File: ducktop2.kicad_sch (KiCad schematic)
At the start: 0 parts

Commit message: Checkpoint ducktop2 generated schematic baseline
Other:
- added sheet Ham Radio (09_ham_radio.kicad_sch)
- added sheet Intehill Monitor Interface (11_intehill_monitor_interface.kicad_sch)
- added sheet Internal Display (10_internal_display.kicad_sch)
- added sheet Internal Services (08_internal_services.kicad_sch)
- added sheet Keyboard Daughterboard (12_keyboard_daughterboard.kicad_sch)
- added sheet Maker MCU (14_maker_mcu.kicad_sch)
- added sheet Mu Carrier (03_mu_carrier.kicad_sch)
- added sheet Power Inputs (05_power_inputs.kicad_sch)
- added sheet Radio Audio Codec (13_radio_audio_codec.kicad_sch)
- added sheet Radio/OLED/GNSS (07_radio_oled_gps.kicad_sch)
- added sheet TCP0 External HDMI (06_tcp0_external_hdmi.kicad_sch)
- added sheet USB-C Hub I/O (04_usb_c_io.kicad_sch)
- sheet EC & MCU ports: added AUX_DC_ADC, FAN_PWM, FAN_TACH, GNSS_EXTINT, GNSS_PPS, GNSS_RESET_N, GNSS_UART_RX, GNSS_UART_TX, KB_COL0, KB_COL1, KB_COL10, KB_COL11, KB_COL12, KB_COL13, KB_COL14, KB_COL15, KB_COL2, KB_COL3, KB_COL4, KB_COL5, KB_COL6, KB_COL7, KB_COL8, KB_COL9, KB_ROW0, KB_ROW1, KB_ROW2, KB_ROW3, KB_ROW4, KB_ROW5, KB_ROW6, KB_ROW7, LCD_BL_EN, LCD_BL_PWM, LID_CLOSED_N, MU_PWRBTN_N, MU_RSTBTN_N, OLED_RESET_N, PANEL_PWR_EN, PANEL_RESET_N, RADIO_AUDIO_SEL, RADIO_GPIO0, RADIO_UHF_PD_N, RADIO_UHF_PTT_N, RADIO_UHF_RF_SEL, RADIO_UHF_SQL, RADIO_UHF_UART_RX, RADIO_UHF_UART_TX, RADIO_VHF_PD_N, RADIO_VHF_PTT_N, RADIO_VHF_RF_SEL, RADIO_VHF_SQL, RADIO_VHF_UART_RX, RADIO_VHF_UART_TX, THERM_MU_ADC, THERM_SKIN_ADC, TOUCH_INT_N, TOUCH_RESET_N, TPAD_INT_N, TPAD_RESET_N, WIFI_W_DISABLE1_N, WIFI_W_DISABLE2_N; removed none
- sheet Power & Battery ports: added AUX_DC_ADC, MCU_3V3; removed none

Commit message: Publish the current Ducktop2 design
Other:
- sheet USB-C Hub I/O renamed Native USB-C I/O
- removed sheet Intehill Monitor Interface
- removed sheet Internal Display
- removed sheet Keyboard Daughterboard
- added sheet Gigabit Ethernet (16_gigabit_ethernet.kicad_sch)
- added sheet Keyboard Mainboard FFC (12_keyboard_interface.kicad_sch)
- added sheet System Audio (15_system_audio.kicad_sch)
- sheet EC & MCU ports: added AON_FAULT_N, AUDIO_AMP_EC_EN, AUDIO_MIC_EN, AUX_FAULT_N, AUX_PGOOD, CASE_PWRBTN_N, CHG_ENABLE, EC_AON_IN, INTERNAL_USB_VBUS_FAULT_N, KB_RGB_DATA_3V3, KB_RGB_FAULT_N, KB_RGB_PWR_EN, MAIN_AUX_VALID_N, MAIN_USB_VALID_N, MU_12V_ENABLE, MU_12V_PG, MU_S0_HIGH, PACK_FAULT_N, PACK_RETRY_PULSE, PD1_EFUSE_FAULT_N, PD1_PATH_EN, PD1_VALID_N, PD2_EFUSE_FAULT_N, PD2_PATH_EN, PD2_VALID_N, PD3_EFUSE_FAULT_N, PD3_PATH_EN, PD3_VALID_N, PMIC_QON_ASSERT, RADIO_UHF_RF_SEL_3V3, RADIO_VHF_RF_SEL_3V3, SERVICE_MUX_RESET_N, TRACKPAD_FAULT_N, WIFI_W_DISABLE1_N_EC, WIFI_W_DISABLE2_N_EC; removed CHG_CE_N, KB_COL15, LCD_BL_EN, LCD_BL_PWM, OLED_RESET_N, PANEL_PWR_EN, PANEL_RESET_N, PMIC_QON, RADIO_UHF_RF_SEL, RADIO_VHF_RF_SEL, TOUCH_INT_N, TOUCH_RESET_N, TPAD_INT_N, TPAD_RESET_N, VSYS, WIFI_W_DISABLE1_N, WIFI_W_DISABLE2_N
- sheet Ham Radio ports: added RADIO_UHF_RF_SEL_3V3, RADIO_VHF_RF_SEL_3V3; removed RADIO_UHF_RF_SEL, RADIO_VHF_RF_SEL
- sheet Internal Services ports: added INTERNAL_USB_VBUS_VALID, MU_12V, MU_HOST_ACTIVE, TRACKPAD_FAULT_N; removed I2C_SCL, I2C_SDA, LCD_BL_EN, LCD_BL_PWM, PANEL_PWR_EN, PANEL_RESET_N, TOUCH_INT_N, TOUCH_RESET_N, TOUCH_USB_DM, TOUCH_USB_DP, TPAD_INT_N, TPAD_RESET_N
- sheet Maker MCU ports: added INTERNAL_USB_VBUS_VALID; removed none
- sheet Mu Carrier ports: added GBE_CLKREQ_N, GBE_HOST_RX_N, GBE_HOST_RX_P, GBE_HOST_TX_N, GBE_HOST_TX_P, GBE_REFCLK_N, GBE_REFCLK_P, INTERNAL_USB_VBUS_FAULT_N, INTERNAL_USB_VBUS_VALID, MCU_3V3, MU_12V, MU_12V_ENABLE, MU_12V_PG, MU_HOST_ACTIVE, MU_S0_HIGH, MU_USB_OC_N, PCIE_3V3, USBC1_DM, USBC1_DP, USBC1_SSRX_N, USBC1_SSRX_P, USBC1_SSTX_N, USBC1_SSTX_P, USBC2_DM, USBC2_DP, USBC2_SSRX_N, USBC2_SSRX_P, USBC2_SSTX_N, USBC2_SSTX_P; removed DDIB_DDC_SCL, DDIB_DDC_SDA, DDIB_HPD, DDIB_TX0_N, DDIB_TX0_P, DDIB_TX1_N, DDIB_TX1_P, DDIB_TX2_N, DDIB_TX2_P, DDIB_TX3_N, DDIB_TX3_P, HUB1_DM, HUB1_DP, HUB1_OC_N, HUB1_PE, HUB1_SSRX_N, HUB1_SSRX_P, HUB1_SSTX_N, HUB1_SSTX_P, HUB2_DM, HUB2_DP, HUB2_OC_N, HUB2_PE, HUB2_SSRX_N, HUB2_SSRX_P, HUB2_SSTX_N, HUB2_SSTX_P, TOUCH_USB_DM, TOUCH_USB_DP
- sheet Native USB-C I/O ports: added MU_HOST_ACTIVE, MU_USB_OC_N, USBC1_DM, USBC1_DP, USBC1_SSRX_N, USBC1_SSRX_P, USBC1_SSTX_N, USBC1_SSTX_P, USBC2_DM, USBC2_DP, USBC2_SSRX_N, USBC2_SSRX_P, USBC2_SSTX_N, USBC2_SSTX_P; removed HUB1_DM, HUB1_DP, HUB1_OC_N, HUB1_PE, HUB1_SSRX_N, HUB1_SSRX_P, HUB1_SSTX_N, HUB1_SSTX_P, HUB2_DM, HUB2_DP, HUB2_OC_N, HUB2_PE, HUB2_SSRX_N, HUB2_SSRX_P, HUB2_SSTX_N, HUB2_SSTX_P
- sheet Power & Battery ports: added AON_FAULT_N, AUX_FAULT_N, AUX_PGOOD, CASE_PWRBTN_N, CHG_ENABLE, EC_AON_IN, MAIN_AUX_VALID_N, MAIN_USB_VALID_N, MU_PWRBTN_N, PACK_FAULT_N, PACK_RETRY_PULSE, PD1_VBUS_RAW, PD2_VBUS_RAW, PD3_VBUS_RAW, PMIC_QON_ASSERT, USB_PD_SELECTED; removed CHG_CE_N, PMIC_QON, USB_DM1, USB_DP1, VBUS_PD1, VBUS_PD2, VBUS_PD3
- sheet Power Inputs ports: added MCU_3V3, PD1_EFUSE_FAULT_N, PD1_I2C_SCL, PD1_I2C_SDA, PD1_PATH_EN, PD1_VALID_N, PD1_VBUS_RAW, PD2_EFUSE_FAULT_N, PD2_I2C_SCL, PD2_I2C_SDA, PD2_PATH_EN, PD2_VALID_N, PD2_VBUS_RAW, PD3_EFUSE_FAULT_N, PD3_I2C_SCL, PD3_I2C_SDA, PD3_PATH_EN, PD3_VALID_N, PD3_VBUS_RAW, USB_PD_SELECTED; removed USB_DM1, USB_DP1, VBUS_PD1, VBUS_PD2, VBUS_PD3
- sheet Radio Audio Codec ports: added MCU_3V3, RADIO_CODEC_USB_DM, RADIO_CODEC_USB_DP, RADIO_CODEC_USB_VBUS, RADIO_UHF_PTT_N, RADIO_VHF_PTT_N; removed AUDIO_USB_DM, AUDIO_USB_DP, SYS_5V
- sheet Radio/OLED/GNSS ports: added PCIE_3V3, PD1_I2C_SCL, PD1_I2C_SDA, PD2_I2C_SCL, PD2_I2C_SDA, PD3_I2C_SCL, PD3_I2C_SDA, SERVICE_MUX_RESET_N, WIFI_W_DISABLE1_N_EC, WIFI_W_DISABLE2_N_EC; removed OLED_RESET_N, SYS_3V3, WIFI_W_DISABLE1_N, WIFI_W_DISABLE2_N
- sheet TCP0 External HDMI ports: added MU_HOST_ACTIVE, SYS_3V3; removed none

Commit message: Finish USB-C policy and split out radio board
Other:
- sheet Radio/OLED/GNSS renamed Wi-Fi/Bluetooth & OLEDs
- removed sheet Ham Radio
- removed sheet Radio Audio Codec
- added sheet Optional Radio Daughterboard Interface (09_radio_daughterboard_interface.kicad_sch)
- sheet EC & MCU ports: added PD1_TCPC_IRQ_N, PD2_TCPC_IRQ_N, PD_PROTECT_FAULT_N, RADIO_DB_FAULT_N, RADIO_DB_PG, RADIO_DB_PRESENT_N, RADIO_DB_PWR_EN; removed PD3_EFUSE_FAULT_N, PD3_PATH_EN, PD3_VALID_N, RADIO_AUDIO_SEL, RADIO_GPIO0
- sheet Mu Carrier ports: added PD_PROTECT_FAULT_N; removed MU_USB_OC_N
- sheet Native USB-C I/O ports: added HUB_DS1_DM, HUB_DS1_DP, HUB_DS1_SSRX_N, HUB_DS1_SSRX_P, HUB_DS1_SSTX_N, HUB_DS1_SSTX_P, INTERNAL_USB_VBUS_VALID, USB_PORT_5V, VSYS; removed MU_HOST_ACTIVE, MU_USB_OC_N, SYS_5V, USBC1_DM, USBC1_DP, USBC1_SSRX_N, USBC1_SSRX_P, USBC1_SSTX_N, USBC1_SSTX_P
- sheet Power & Battery ports: added none; removed PD3_VBUS_RAW
- sheet Power Inputs ports: added HUB_DS1_DM, HUB_DS1_DP, HUB_DS1_SSRX_N, HUB_DS1_SSRX_P, HUB_DS1_SSTX_N, HUB_DS1_SSTX_P, PD1_TCPC_IRQ_N, PD2_TCPC_IRQ_N, PD_PROTECT_FAULT_N, SYS_3V3, USBC1_DM, USBC1_DP, USBC1_SSRX_N, USBC1_SSRX_P, USBC1_SSTX_N, USBC1_SSTX_P, USB_PORT_5V; removed PD3_EFUSE_FAULT_N, PD3_I2C_SCL, PD3_I2C_SDA, PD3_PATH_EN, PD3_VALID_N, PD3_VBUS_RAW
- sheet System Audio ports: added RADIO_CODEC_USB_DM_HOST, RADIO_CODEC_USB_DP_HOST, RADIO_CODEC_USB_VBUS_HOST; removed RADIO_CODEC_USB_DM, RADIO_CODEC_USB_DP, RADIO_CODEC_USB_VBUS
- sheet Wi-Fi/Bluetooth & OLEDs ports: added none; removed GNSS_EXTINT, GNSS_PPS, GNSS_RESET_N, GNSS_UART_RX, GNSS_UART_TX, PD3_I2C_SCL, PD3_I2C_SDA, RADIO_GPIO0

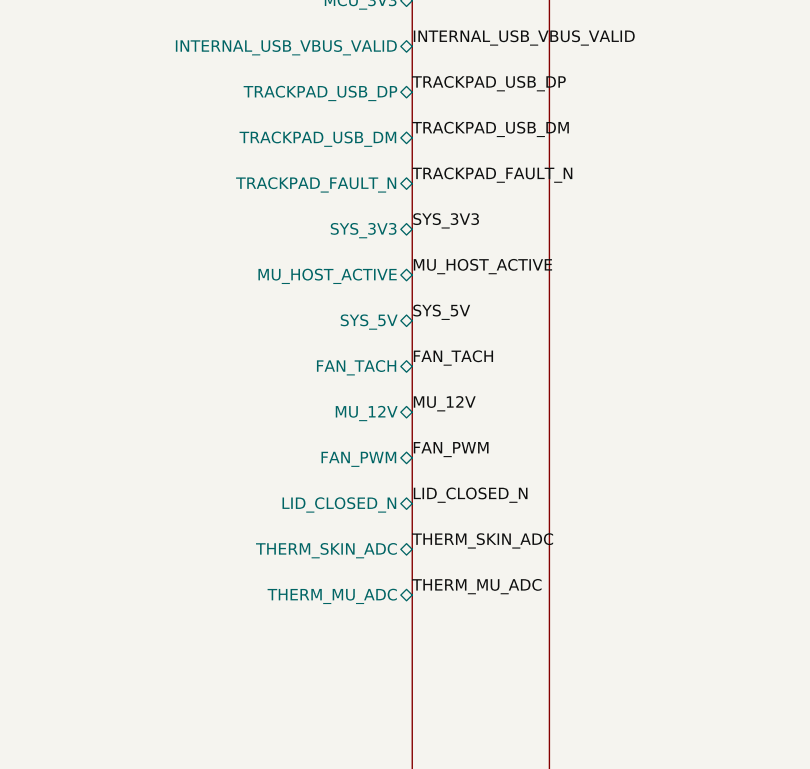
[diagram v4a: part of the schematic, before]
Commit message: Wire the trackpad directly over USB2 and record audit holds
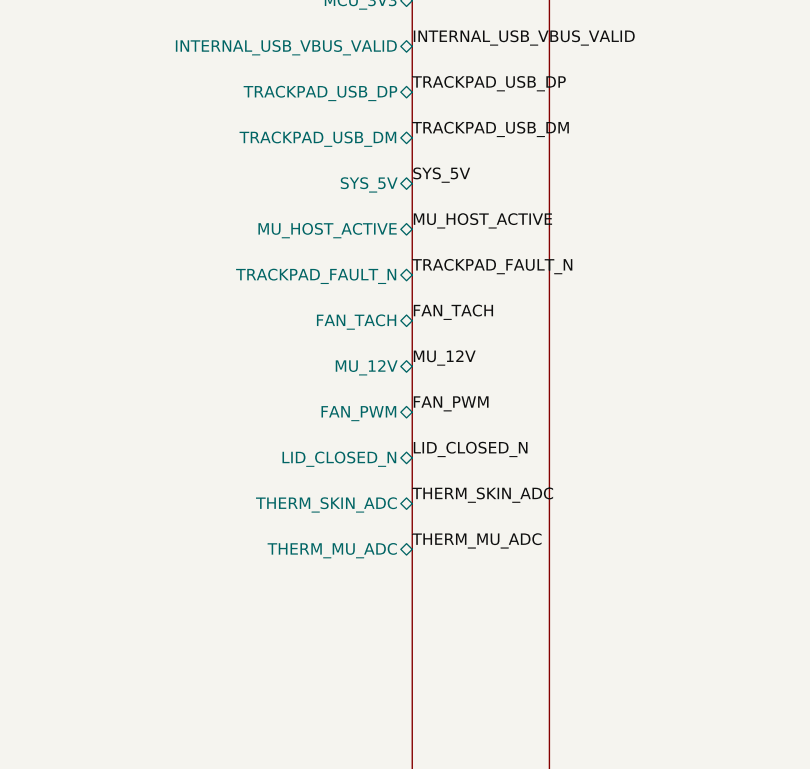
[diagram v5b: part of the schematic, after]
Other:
- sheet Internal Services ports: added none; removed SYS_3V3
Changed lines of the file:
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@@
+    (effects (font (size 1.27 1.27)) (justify left))
+  )
+  (pin "SYS_5V" bidirectional
+    (at 405.13 435.61 0)
+    (effects (font (size 1.27 1.27)) (justify left))
+  )
+  (pin "MU_HOST_ACTIVE" bidirectional
+    (at 405.13 440.69 0)
     (effects (font (size 1.27 1.27)) (justify left))
   )
   (pin "TRACKPAD_FAULT_N" bidirectional
-    (at 405.13 435.61 0)
-    (effects (font (size 1.27 1.27)) (justify left))
-  )
-  (pin "SYS_3V3" bidirectional
-    (at 405.13 440.69 0)
-    (effects (font (size 1.27 1.27)) (justify left))
-  )
-  (pin "MU_HOST_ACTIVE" bidirectional
     (at 405.13 445.77 0)
     (effects (font (size 1.27 1.27)) (justify left))
   )
-  (pin "SYS_5V" bidirectional
+  (pin "FAN_TACH" bidirectional
     (at 405.13 450.85 0)
     (effects (font (size 1.27 1.27)) (justify left))
   )
-  (pin "FAN_TACH" bidirectional
+  (pin "MU_12V" bidirectional
     (at 405.13 455.93 0)
     (effects (font (size 1.27 1.27)) (justify left))
   )
-  (pin "MU_12V" bidirectional
+  (pin "FAN_PWM" bidirectional
     (at 405.13 461.01 0)
     (effects (font (size 1.27 1.27)) (justify left))
   )
-  (pin "FAN_PWM" bidirectional
+  (pin "LID_CLOSED_N" bidirectional
     (at 405.13 466.09 0)
     (effects (font (size 1.27 1.27)) (justify left))
   )
-  (pin "LID_CLOSED_N" bidirectional
+  (pin "THERM_SKIN_ADC" bidirectional
     (at 405.13 471.17 0)
     (effects (font (size 1.27 1.27)) (justify left))
   )
-  (pin "THERM_SKIN_ADC" bidirectional
+  (pin "THERM_MU_ADC" bidirectional
     (at 405.13 476.25 0)
-    (effects (font (size 1.27 1.27)) (justify left))
-  )
-  (pin "THERM_MU_ADC" bidirectional
-    (at 405.13 481.33 0)
     (effects (font (size 1.27 1.27)) (justify left))
   )
@@
 )
 (label "THERM_SKIN_ADC"
-  (at 405.13 476.25 0)
+  (at 405.13 471.17 0)
   (effects (font (size 1.27 1.27)) (justify left bottom))
 )
@@
 )
 (label "FAN_TACH"
-  (at 405.13 455.93 0)
+  (at 405.13 450.85 0)
   (effects (font (size 1.27 1.27)) (justify left bottom))
 )
@@
 )
 (label "THERM_MU_ADC"
-  (at 405.13 481.33 0)
+  (at 405.13 476.25 0)
   (effects (font (size 1.27 1.27)) (justify left bottom))
 )
@@
 )
 (label "TRACKPAD_FAULT_N"
-  (at 405.13 435.61 0)
+  (at 405.13 445.77 0)
   (effects (font (size 1.27 1.27)) (justify left bottom))
 )
@@
 )
 (label "FAN_PWM"
-  (at 405.13 466.09 0)
+  (at 405.13 461.01 0)
   (effects (font (size 1.27 1.27)) (justify left bottom))
 )
@@
 )
 (label "LID_CLOSED_N"
-  (at 405.13 471.17 0)
+  (at 405.13 466.09 0)
   (effects (font (size 1.27 1.27)) (justify left bottom))
 )
@@
 )
 (label "SYS_5V"
-  (at 405.13 450.85 0)
+  (at 405.13 435.61 0)
   (effects (font (size 1.27 1.27)) (justify left bottom))
 )
@@
 )
 (label "SYS_3V3"
-  (at 405.13 440.69 0)
-  (effects (font (size 1.27 1.27)) (justify left bottom))
-)
-(label "SYS_3V3"
   (at 814.07 355.6 0)
   (effects (font (size 1.27 1.27)) (justify left bottom))
@@
 )
 (label "MU_12V"
-  (at 405.13 461.01 0)
+  (at 405.13 455.93 0)
   (effects (font (size 1.27 1.27)) (justify left bottom))
 )
@@
 )
 (label "MU_HOST_ACTIVE"
-  (at 405.13 445.77 0)
-  (effects (font (size 1.27 1.27)) (justify left bottom))
-)
+  (at 405.13 440.69 0)
+  (effects (font (size 1.27 1.27)) (justify left bottom))
+)

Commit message: Add rear 3.5mm headphone jack with plug-detect speaker mute (sheet 15)
Add the missing headphone output the user-verified behavior requires (row 11): rear CUI SJ1-3535NG stereo jack driven by a TPA6130A2RTJR DirectPath headphone amp, with automatic plug-detect speaker muting like a normal laptop.

- U425 TPA6130A2 (I2C @0x60, fixed): single-ended inputs from PCM2900C DAC_VOUT_L/R via 0.47u coupling (INM signal, INP AC-grounded per datasheet 9.2.2.1); capless ground-referenced HPLEFT/HPRIGHT outputs to jack T/R. Charge-pump flying + CPVSS + VDD bypass per 9.2.2.2/3.
- J422 SJ1-3535NG: RN ring normalling switch is plug detect (unplugged shorts RN to R = amp 0V -> low; plugged floats -> high).
- HP_DETECT is read by the EC on U44 (TCA9539 source manager) recovered spare input pin 6 (SOURCE_MGR_SPARE1 repurposed) with R782 100k pull-up to MCU_3V3. On plug-in the EC drives AUDIO_AMP_EC_EN low (U421 AND gate mutes the TPA2012D2 speaker amp) and I2C-unmutes U425.
- /SD tied to MU_HOST_ACTIVE so U425 is in hardware shutdown (0.4uA) outside S0; power-on default is muted with outputs disabled (fail-safe OFF until EC firmware enables over I2C).
- Datasheet-verified: TPA6130A2 is I2C-controlled (no G0/G1 hardware gain); reuses the TPA2012D2 WQFN-20-1EP 4x4mm EP2.7x2.7 footprint; AudioJack3_SwitchTR symbol matches the SJ1-3535NG 5-pad footprint (T/R/S/TN/RN).
- Contracts (verify_design_contracts, generate_pin_review_table x2, verify_schematic_closure) updated SPARE1->HP_DETECT. Added TPA6130A2 to sym-lib-table+LIBMAP.
- Enlarged System Audio root sheet block 60->85mm so all 14 hier pins fit; KiCad clamps sheet pins that overflow the block to the rectangle edge and merges them, which otherwise collapses I2C_SCL/HP_DETECT/AUDIO_MIC_EN into one net.
- ERC 0 errors/27 intentional warnings; schematic closure 1580/0; pin review 2603/2603.
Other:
- sheet EC & MCU ports: added HP_DETECT; removed none
- sheet System Audio ports: added HP_DETECT, I2C_SCL, I2C_SDA, MU_HOST_ACTIVE; removed none
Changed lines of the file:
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@@
+    (effects (font (size 1.27 1.27)) (justify left))
+  )
+  (pin "HP_DETECT" bidirectional
+    (at 219.71 445.77 0)
     (effects (font (size 1.27 1.27)) (justify left))
   )
   (pin "PD1_EFUSE_FAULT_N" bidirectional
-    (at 219.71 445.77 0)
+    (at 219.71 450.85 0)
     (effects (font (size 1.27 1.27)) (justify left))
   )
   (pin "PD2_EFUSE_FAULT_N" bidirectional
-    (at 219.71 450.85 0)
+    (at 219.71 455.93 0)
     (effects (font (size 1.27 1.27)) (justify left))
   )
   (pin "PACK_FAULT_N" bidirectional
-    (at 219.71 455.93 0)
+    (at 219.71 461.01 0)
     (effects (font (size 1.27 1.27)) (justify left))
   )
   (pin "AUX_FAULT_N" bidirectional
-    (at 219.71 461.01 0)
+    (at 219.71 466.09 0)
     (effects (font (size 1.27 1.27)) (justify left))
   )
   (pin "PACK_RETRY_PULSE" bidirectional
-    (at 219.71 466.09 0)
+    (at 219.71 471.17 0)
     (effects (font (size 1.27 1.27)) (justify left))
   )
   (pin "AUX_PGOOD" bidirectional
-    (at 219.71 471.17 0)
+    (at 219.71 476.25 0)
     (effects (font (size 1.27 1.27)) (justify left))
   )
   (pin "MAIN_USB_VALID_N" bidirectional
-    (at 219.71 476.25 0)
+    (at 219.71 481.33 0)
     (effects (font (size 1.27 1.27)) (justify left))
   )
   (pin "MAIN_AUX_VALID_N" bidirectional
-    (at 219.71 481.33 0)
+    (at 219.71 486.41 0)
     (effects (font (size 1.27 1.27)) (justify left))
   )
   (pin "AON_FAULT_N" bidirectional
-    (at 219.71 486.41 0)
+    (at 219.71 491.49 0)
     (effects (font (size 1.27 1.27)) (justify left))
   )
   (pin "RADIO_DB_PG" bidirectional
-    (at 219.71 491.49 0)
+    (at 219.71 496.57 0)
     (effects (font (size 1.27 1.27)) (justify left))
   )
   (pin "RADIO_DB_FAULT_N" bidirectional
-    (at 219.71 496.57 0)
+    (at 219.71 501.65 0)
     (effects (font (size 1.27 1.27)) (justify left))
   )
   (pin "RADIO_DB_PRESENT_N" bidirectional
-    (at 219.71 501.65 0)
+    (at 219.71 506.73 0)
     (effects (font (size 1.27 1.27)) (justify left))
   )
   (pin "SERVICE_MUX_RESET_N" bidirectional
-    (at 219.71 506.73 0)
+    (at 219.71 511.81 0)
     (effects (font (size 1.27 1.27)) (justify left))
   )
@@
 (sheet
   (at 679.45 330.2)
-  (size 134.62 59.69)
+  (size 134.62 85.09)
   (stroke (width 0.1524) (type solid))
   (fill (color 0 0 0 0.0))
@@
   )
   (property "Sheetfile" "15_system_audio.kicad_sch"
-    (at 679.45 391.16 0)
+    (at 679.45 416.56 0)
     (effects (font (size 1.27 1.27)) (justify left top))
   )
@@
     (effects (font (size 1.27 1.27)) (justify left))
   )
+  (pin "MU_HOST_ACTIVE" bidirectional
+    (at 814.07 381 0)
+    (effects (font (size 1.27 1.27)) (justify left))
+  )
+  (pin "I2C_SDA" bidirectional
+    (at 814.07 386.08 0)
+    (effects (font (size 1.27 1.27)) (justify left))
+  )
+  (pin "I2C_SCL" bidirectional
+    (at 814.07 391.16 0)
+    (effects (font (size 1.27 1.27)) (justify left))
+  )
+  (pin "HP_DETECT" bidirectional
+    (at 814.07 396.24 0)
+    (effects (font (size 1.27 1.27)) (justify left))
+  )
   (pin "AUDIO_MIC_EN" bidirectional
-    (at 814.07 381 0)
+    (at 814.07 401.32 0)
     (effects (font (size 1.27 1.27)) (justify left))
   )
@@
 )
 (label "PACK_FAULT_N"
-  (at 219.71 455.93 0)
+  (at 219.71 461.01 0)
   (effects (font (size 1.27 1.27)) (justify left bottom))
 )
@@
 )
 (label "PACK_RETRY_PULSE"
-  (at 219.71 466.09 0)
+  (at 219.71 471.17 0)
   (effects (font (size 1.27 1.27)) (justify left bottom))
 )
@@
   (effects (font (size 1.27 1.27)) (justify left bottom))
 )
+(label "I2C_SCL"
+  (at 814.07 391.16 0)
+  (effects (font (size 1.27 1.27)) (justify left bottom))
+)
 (label "I2C_SDA"
   (at 90.17 69.85 0)
@@
   (effects (font (size 1.27 1.27)) (justify left bottom))
 )
+(label "I2C_SDA"
+  (at 814.07 386.08 0)
+  (effects (font (size 1.27 1.27)) (justify left bottom))
+)
 (label "CHG_INT_N"
   (at 90.17 74.93 0)
@@
 )
 (label "AUX_FAULT_N"
-  (at 219.71 461.01 0)
+  (at 219.71 466.09 0)
   (effects (font (size 1.27 1.27)) (justify left bottom))
 )
@@
 )
 (label "AUX_PGOOD"
-  (at 219.71 471.17 0)
+  (at 219.71 476.25 0)
   (effects (font (size 1.27 1.27)) (justify left bottom))
 )
@@
 )
 (label "MAIN_USB_VALID_N"
-  (at 219.71 476.25 0)
+  (at 219.71 481.33 0)
   (effects (font (size 1.27 1.27)) (justify left bottom))
 )
@@
 )
 (label "MAIN_AUX_VALID_N"
-  (at 219.71 481.33 0)
+  (at 219.71 486.41 0)
   (effects (font (size 1.27 1.27)) (justify left bottom))
 )
@@
 )
 (label "AON_FAULT_N"
-  (at 219.71 486.41 0)
+  (at 219.71 491.49 0)
   (effects (font (size 1.27 1.27)) (justify left bottom))
 )
@@
 )
 (label "AUDIO_MIC_EN"
-  (at 814.07 381 0)
+  (at 814.07 401.32 0)
   (effects (font (size 1.27 1.27)) (justify left bottom))
 )
@@
   (effects (font (size 1.27 1.27)) (justify left bottom))
 )
+(label "HP_DETECT"
+  (at 219.71 445.77 0)
+  (effects (font (size 1.27 1.27)) (justify left bottom))
+)
+(label "HP_DETECT"
+  (at 814.07 396.24 0)
+  (effects (font (size 1.27 1.27)) (justify left bottom))
+)
 (label "PD1_EFUSE_FAULT_N"
-  (at 219.71 445.77 0)
+  (at 219.71 450.85 0)
   (effects (font (size 1.27 1.27)) (justify left bottom))
 )
@@
 )
 (label "PD2_EFUSE_FAULT_N"
-  (at 219.71 450.85 0)
+  (at 219.71 455.93 0)
   (effects (font (size 1.27 1.27)) (justify left bottom))
 )
@@
 )
 (label "RADIO_DB_PG"
-  (at 219.71 491.49 0)
+  (at 219.71 496.57 0)
   (effects (font (size 1.27 1.27)) (justify left bottom))
 )
@@
 )
 (label "RADIO_DB_FAULT_N"
-  (at 219.71 496.57 0)
+  (at 219.71 501.65 0)
   (effects (font (size 1.27 1.27)) (justify left bottom))
 )
@@
 )
 (label "RADIO_DB_PRESENT_N"
-  (at 219.71 501.65 0)
+  (at 219.71 506.73 0)
   (effects (font (size 1.27 1.27)) (justify left bottom))
 )
@@
 )
 (label "SERVICE_MUX_RESET_N"
-  (at 219.71 506.73 0)
+  (at 219.71 511.81 0)
   (effects (font (size 1.27 1.27)) (justify left bottom))
 )
@@
   (effects (font (size 1.27 1.27)) (justify left bottom))
 )
+(label "MU_HOST_ACTIVE"
+  (at 814.07 381 0)
+  (effects (font (size 1.27 1.27)) (justify left bottom))
+)
